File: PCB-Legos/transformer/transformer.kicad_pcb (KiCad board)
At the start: 4 copper layers, 22.5 x 10 mm, 3 parts, among them J1 Conn_Coaxial, U1 NCS3-272+

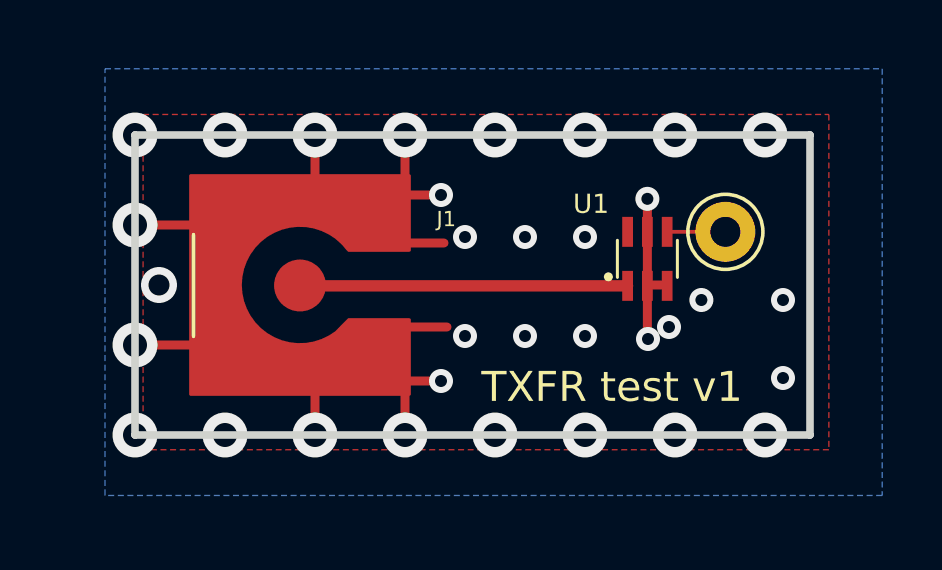
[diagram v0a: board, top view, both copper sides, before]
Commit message: Updated library paths to be more sane, especially for footprints. Then unmasked the vias along the edges so that we can get castellated edges. Also reduced the size of the antenna hole, no reason to be that big.
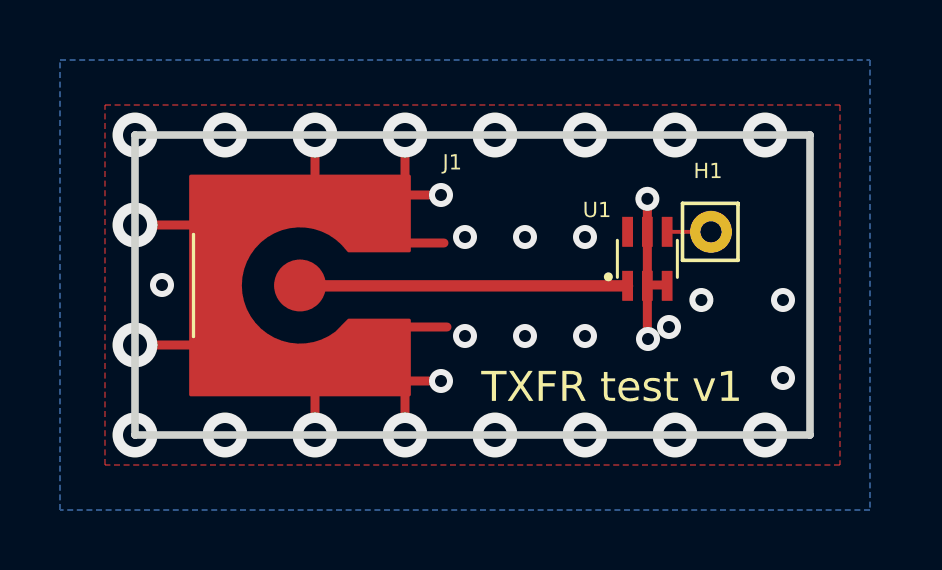
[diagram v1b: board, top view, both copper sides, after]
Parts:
- H1: footprint Connector_Pin:Pin_D1.0mm_L10.0mm -> Connector_Pin:Pin_D0.7mm_L6.5mm_W1.8mm_FlatFork
- J1: footprint footprints:J-Amphenol-132134-10-SMA-F-SMT-vertical -> oresat-footprints:J-Amphenol-132134-10-SMA-F-SMT-vertical
- U1: footprint footprints:Minicircuits-GE0805C-9 -> oresat-footprints:U-Minicircuits-GE0805C-9
- moved H1 0.48 mm to (149.2, 98.2)
